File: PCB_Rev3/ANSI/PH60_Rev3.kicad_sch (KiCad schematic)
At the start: 28 parts, among them J1 USB_C_Receptacle_USB2.0_16P, J2 Conn_01x02, U1 XC6206PxxxMR, U2 W25Q16JVSS, U3 RP2040, Y1 Crystal_GND24

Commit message: Wires optimization.
More GND hole still needed...
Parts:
- J1: footprint Connector_USB:USB_C_Receptacle_HCTL_HC-TYPE-C-16P-01A -> PH60:USB-C_16P_HandSolder
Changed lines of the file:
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@@
 			)
 		)
-		(property "Footprint" "Connector_USB:USB_C_Receptacle_HCTL_HC-TYPE-C-16P-01A"
+		(property "Footprint" "PH60:USB-C_16P_HandSolder"
 			(at 52.07 220.98 0)
 			(effects

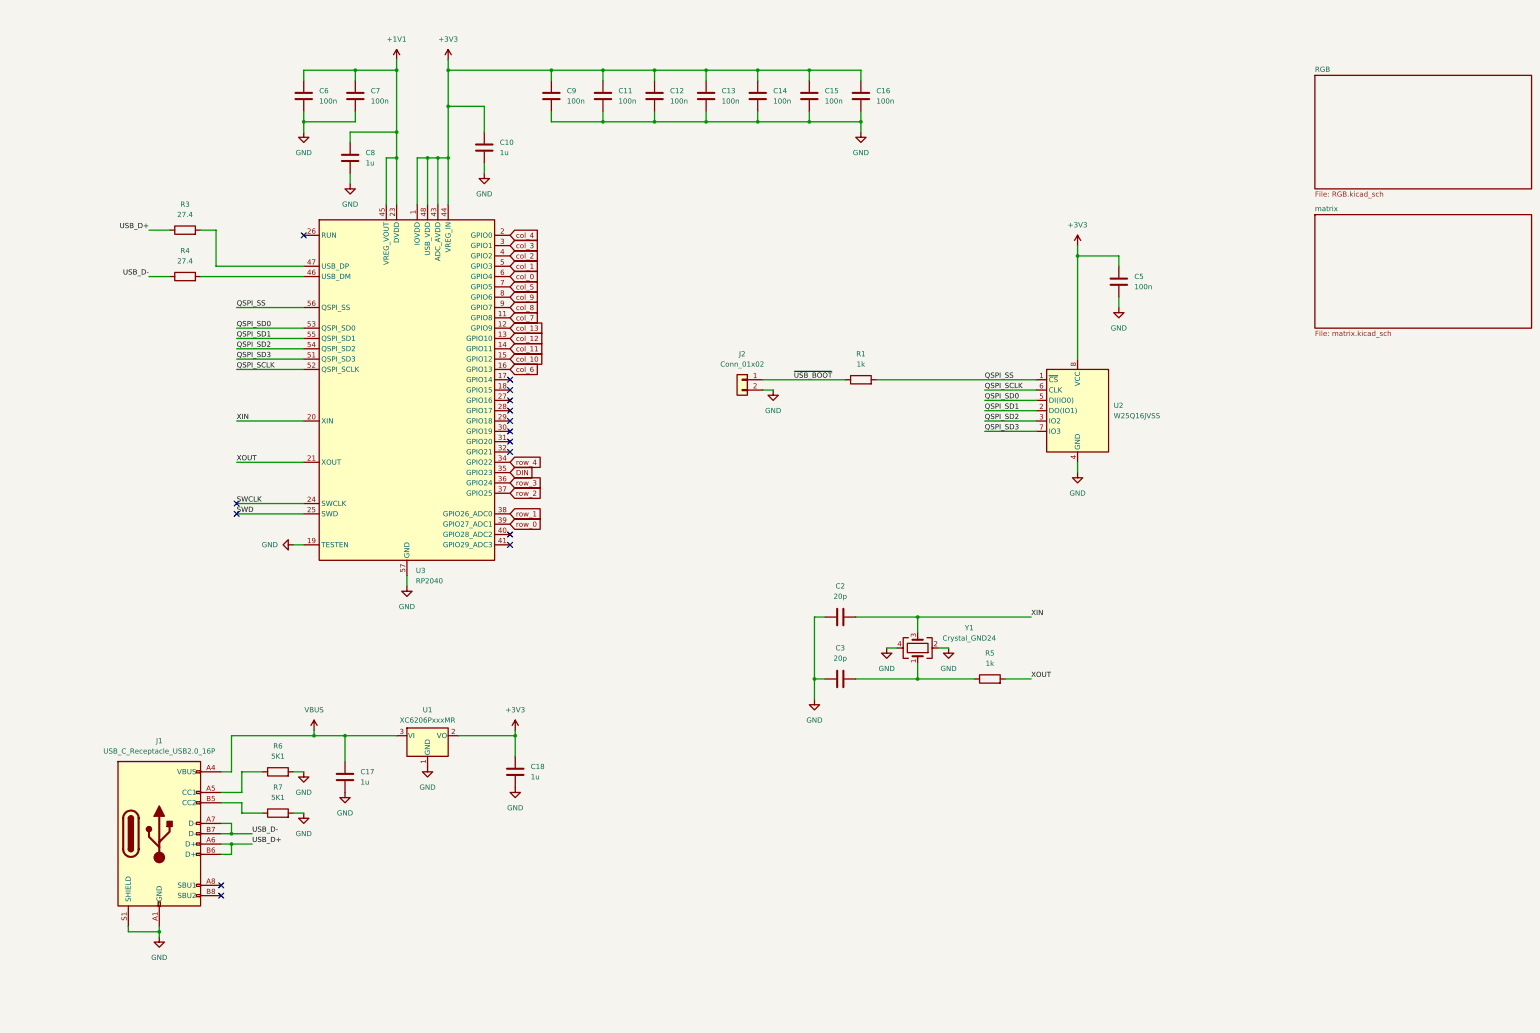
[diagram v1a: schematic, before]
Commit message: Add wireless part
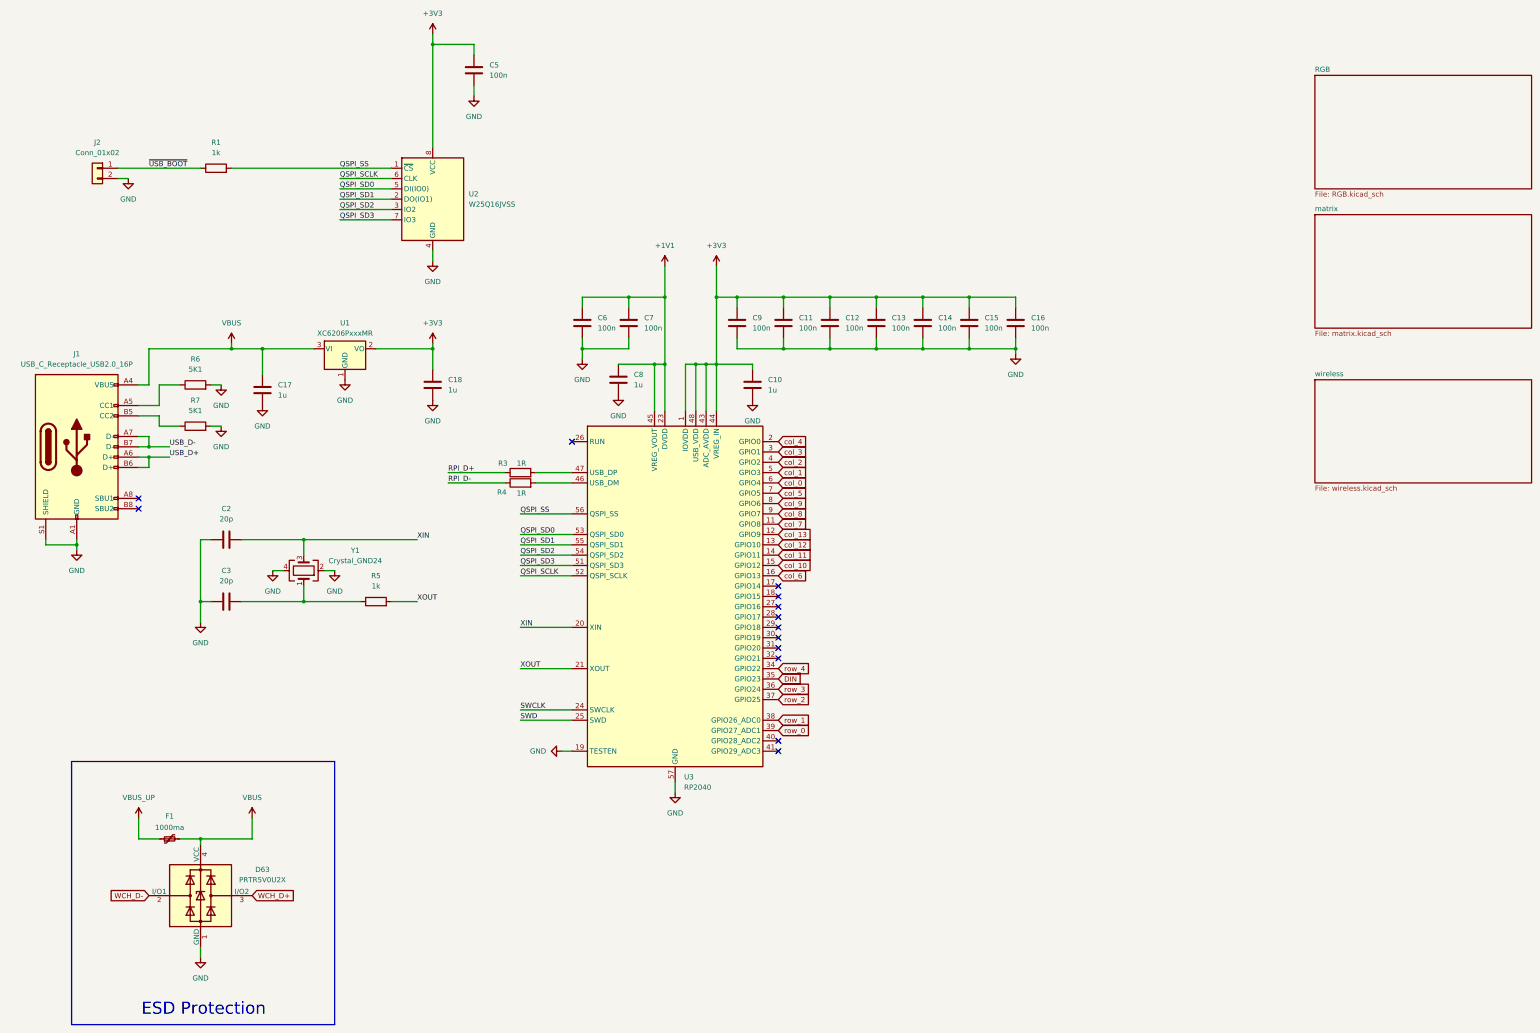
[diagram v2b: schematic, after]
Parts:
- added D63: PRTR5V0U2X, Package_TO_SOT_SMD:SOT-143, symbol Power_Protection:PRTR5V0U2X
- added F1: 1000ma, Fuse:Fuse_0805_2012Metric, symbol Device:Polyfuse_Small
- R3, R4: value 27.4 -> 1R
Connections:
- net GND: now also D63.1 (GND)
- net USB_D+: no longer R3.1
- net USB_D-: no longer R4.1
- net VBUS: now also D63.4 (VCC), F1.2
- new net RPI_D+: R3.1
- new net RPI_D-: R4.1
- new net VBUS_UP: F1.1
- new net WCH_D+: D63.3 (I/O2)
- new net WCH_D-: D63.2 (I/O1)
- no-connect marks 15 -> 13
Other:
- added sheet wireless (wireless.kicad_sch)
- note added: "ESD Protection"
- moved on the sheet: C10, C11, C12, C13, C14, C15, C16, C17, C18, C2, C3, C5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

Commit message: Finish board design
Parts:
- removed U1: XC6206PxxxMR, Package_TO_SOT_SMD:SOT-23-3, symbol Regulator_Linear:XC6206PxxxMR
- added BT1: Battery, Connector_Molex:Molex_PicoBlade_53261-0271_1x02-1MP_P1.25mm_Horizontal, symbol Device:Battery
- added C14: 4.7u, Capacitor_SMD:C_0402_1005Metric, symbol Device:C
- added C15: 10u, Capacitor_SMD:C_0402_1005Metric, symbol Device:C
- added J3: Conn_01x02_Pin, symbol Connector:Conn_01x02_Pin
- added J4: Conn_01x02_Pin, Connector_PinHeader_1.27mm:PinHeader_1x02_P1.27mm_Vertical, symbol Connector:Conn_01x02_Pin
- added L1, L2: 2.2uH, Inductor_SMD:L_Changjiang_FNR252012S, symbol Device:L
- added R10: 33k, PCM_Resistor_SMD_AKL:R_0402_1005Metric, symbol Device:R
- added R11: 10k, PCM_Resistor_SMD_AKL:R_0402_1005Metric, symbol Device:R
- added R12, R7: 100k, PCM_Resistor_SMD_AKL:R_0402_1005Metric, symbol Device:R
- added R6: 442k, PCM_Resistor_SMD_AKL:R_0402_1005Metric, symbol Device:R
- added R9: 1k, PCM_Resistor_SMD_AKL:R_0402_1005Metric, symbol Device:R
- added SW1: SW_SPDT_321, PCM_marbastlib-various:SW_MSK12C02-HB, symbol Switch:SW_SPDT_321
- added U1: TLV62569DBV, Package_TO_SOT_SMD:SOT-23-5, symbol Regulator_Switching:TLV62569DBV
- added U4: ETA6093, Package_TO_SOT_SMD:SOT-23-5, symbol ETA6093:ETA6093
- C17: value 1u -> 10u
- C18: value 1u -> 22u
- R1: renamed from R6; footprint Resistor_SMD:R_0402_1005Metric -> PCM_Resistor_SMD_AKL:R_0402_1005Metric
- R2: renamed from R7; footprint Resistor_SMD:R_0402_1005Metric -> PCM_Resistor_SMD_AKL:R_0402_1005Metric
- R3, R4, R5: footprint Resistor_SMD:R_0402_1005Metric -> PCM_Resistor_SMD_AKL:R_0402_1005Metric
- R8: renamed from R1; footprint Resistor_SMD:R_0402_1005Metric -> PCM_Resistor_SMD_AKL:R_0402_1005Metric
- renumbered C6 to C1, C8 to C10, C10 to C11, C2 to C12, C3 to C13, C5 to C16, C7 to C2, C9 to C3, C11 to C4, C12 to C5, C13 to C6, C14 to C7, C15 to C8, C16 to C9, D63 to D1, U3 to U2, U2 to U3
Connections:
- net WCH_D+ is gone; now on net USB_D-: D1.3 (I/O2)
- net WCH_D- is gone; now on net USB_D+: D1.2 (I/O1)
- net +3V3: now also C15.1, L1.2, R6.1; no longer C18.1
- net GND: now also BT1.2 (-), C14.2, C15.2, J4.2 (Pin_2), R12.2, R7.2, U1.2 (GND), U4.2 (GND)
- net SWCLK: now also J3.2 (Pin_2)
- net SWD: now also J3.1 (Pin_1)
- net VBUS: now also C18.1, C14.1, R11.2, U1.1 (EN), U1.4 (VIN), U4.1 (OUT); no longer C17.1, J1.A4 (VBUS), J1.A9 (VBUS), J1.B4 (VBUS), J1.B9 (VBUS)
- net VBUS_UP: now also J1.A4 (VBUS), J1.A9 (VBUS), J1.B4 (VBUS), J1.B9 (VBUS)
- net ~{USB_BOOT}: no longer names the net of J2.1 (Pin_1), R8.1
- new net: L1.1, U1.3 (SW)
- new net: R6.2, R7.1, U1.5 (FB)
- new net: C17.1, L2.1, SW1.3 (A), U4.4 (BAT)
- new net: R9.1, U4.3 (LED)
- new net: L2.2, U4.5 (SW)
- new net +BATT: BT1.1 (+), J4.1 (Pin_1), R10.2, SW1.2 (B)
- new net CHRG: R11.1, R9.2
- new net batt_level: R10.1, R12.1
- no-connect marks 13 -> 14
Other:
- note added: "Batt status"
- note added: "Charge & Boost"
- note added: "Crystal"
- note added: "Debug"
- note added: "Flash"
- note added: "RP2040"
- note added: "USB-C"
- note added: "power"
- moved on the sheet: C1, C10, C11, C12, C13, C16, C2, C3, C4, C5, C6, C7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

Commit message: Regroup
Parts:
- removed U3: W25Q16JVSS, Package_SON:Winbond_USON-8-1EP_3x2mm_P0.5mm_EP0.2x1.6mm, symbol Memory_Flash:W25Q16JVSS
- added U6: W25Q16JVSS, Package_SON:Winbond_USON-8-1EP_3x2mm_P0.5mm_EP0.2x1.6mm, symbol Memory_Flash:W25Q16JVSS
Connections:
- net QSPI_SS is gone; now on net RPI_BOOTSEL: R8.2, U2.56 (QSPI_SS)
- net +3V3: now also U6.8 (VCC)
- net GND: now also U6.4 (GND)
- net QSPI_SCLK: now also U6.6 (CLK)
- net QSPI_SD0: now also U6.5 (DI/IO_{0})
- net QSPI_SD1: now also U6.2 (DO/IO_{1})
- net QSPI_SD2: now also U6.3 (~{WP}/IO_{2})
- net QSPI_SD3: now also U6.7 (~{HOLD}/~{RESET}/IO_{3})
- net RPI_RUN: now reaches U2.26 (RUN)
- net RPI_BOOTSEL: now reaches J2.1 (Pin_1), R8.1
- net RPI_BOOTSEL: now also U6.1 (~{CS})
- no-connect marks 14 -> 13
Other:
- moved on the sheet: C14, C16, J2, R8

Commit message: Add files via upload
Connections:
- net +BATT: no longer SW1.2 (B)
- net GND: now also SW1.3 (A)
- net VBUS: now also SW1.1 (C); no longer U1.1 (EN)
- net at C17.1, L2.1, U4.4 (BAT): no longer SW1.3 (A)
- new net RGB: SW1.2 (B), U1.1 (EN)
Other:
- moved on the sheet: C14
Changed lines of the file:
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@@
 	)
 	(junction
-		(at 196.85 49.53)
+		(at 35.56 97.79)
 		(diameter 0)
 		(color 0 0 0 0)
 	)
 	(junction
-		(at 39.37 100.33)
+		(at 196.85 49.53)
 		(diameter 0)
 		(color 0 0 0 0)
@@
 	)
 	(junction
-		(at 80.01 38.1)
+		(at 45.72 102.87)
 		(diameter 0)
 		(color 0 0 0 0)
 	)
 	(junction
-		(at 146.05 53.34)
+		(at 80.01 38.1)
 		(diameter 0)
 		(color 0 0 0 0)
 	)
 	(junction
-		(at 53.34 154.94)
+		(at 146.05 53.34)
 		(diameter 0)
 		(color 0 0 0 0)
 	)
 	(junction
-		(at 39.37 97.79)
+		(at 53.34 154.94)
 		(diameter 0)
 		(color 0 0 0 0)
@@
 	)
 	(junction
+		(at 43.18 116.84)
+		(diameter 0)
+		(color 0 0 0 0)
+	)
+	(junction
 		(at 143.51 53.34)
 		(diameter 0)
@@
 	)
 	(junction
+		(at 33.02 97.79)
+		(diameter 0)
+		(color 0 0 0 0)
+	)
+	(junction
 		(at 226.06 152.4)
 		(diameter 0)
@@
 	(wire
 		(pts
-			(xy 39.37 97.79) (xy 45.72 97.79)
+			(xy 30.48 97.79) (xy 33.02 97.79)
 		)
 		(stroke
@@
 	(wire
 		(pts
-			(xy 39.37 100.33) (xy 39.37 97.79)
-		)
-		(stroke
-			(width 0)
-			(type default)
-		)
-	)
-	(wire
-		(pts
 			(xy 59.69 38.1) (xy 69.85 38.1)
 		)
@@
 	(wire
 		(pts
+			(xy 33.02 97.79) (xy 35.56 97.79)
+		)
+		(stroke
+			(width 0)
+			(type default)
+		)
+	)
+	(wire
+		(pts
 			(xy 80.01 35.56) (xy 80.01 38.1)
 		)
@@
 	(wire
 		(pts
-			(xy 39.37 102.87) (xy 39.37 100.33)
+			(xy 33.02 97.79) (xy 33.02 102.87)
 		)
 		(stroke
@@
 	(wire
 		(pts
+			(xy 35.56 97.79) (xy 35.56 113.03)
+		)
+		(stroke
+			(width 0)
+			(type default)
+		)
+	)
+	(wire
+		(pts
 			(xy 53.34 223.52) (xy 53.34 227.33)
 		)
@@
 	(wire
 		(pts
-			(xy 39.37 116.84) (xy 53.34 116.84)
+			(xy 33.02 116.84) (xy 43.18 116.84)
 		)
 		(stroke
@@
 	(wire
 		(pts
+			(xy 40.64 102.87) (xy 45.72 102.87)
+		)
+		(stroke
+			(width 0)
+			(type default)
+		)
+	)
+	(wire
+		(pts
 			(xy 73.66 237.49) (xy 73.66 234.95)
 		)
@@
 	(wire
 		(pts
+			(xy 43.18 116.84) (xy 53.34 116.84)
+		)
+		(stroke
+			(width 0)
+			(type default)
+		)
+	)
+	(wire
+		(pts
 			(xy 162.56 36.83) (xy 162.56 39.37)
 		)
@@
 	(wire
 		(pts
-			(xy 39.37 100.33) (xy 45.72 100.33)
-		)
-		(stroke
-			(width 0)
-			(type default)
-		)
-	)
-	(wire
-		(pts
 			(xy 63.5 107.95) (xy 71.12 107.95)
 		)
@@
 	(wire
 		(pts
-			(xy 30.48 97.79) (xy 39.37 97.79)
-		)
-		(stroke
-			(width 0)
-			(type default)
-		)
-	)
-	(wire
-		(pts
 			(xy 146.05 36.83) (xy 151.13 36.83)
 		)
@@
 	(wire
 		(pts
-			(xy 39.37 116.84) (xy 39.37 110.49)
+			(xy 33.02 116.84) (xy 33.02 110.49)
 		)
 		(stroke
@@
 	(wire
 		(pts
+			(xy 43.18 113.03) (xy 43.18 116.84)
+		)
+		(stroke
+			(width 0)
+			(type default)
+		)
+	)
+	(wire
+		(pts
+			(xy 45.72 102.87) (xy 45.72 100.33)
+		)
+		(stroke
+			(width 0)
+			(type default)
+		)
+	)
+	(wire
+		(pts
 			(xy 36.83 68.58) (xy 36.83 69.85)
 		)
@@
 	(wire
 		(pts
+			(xy 45.72 107.95) (xy 45.72 102.87)
+		)
+		(stroke
+			(width 0)
+			(type default)
+		)
+	)
+	(wire
+		(pts
 			(xy 226.06 152.4) (xy 226.06 153.67)
 		)
@@
 	(wire
 		(pts
+			(xy 35.56 97.79) (xy 45.72 97.79)
+		)
+		(stroke
+			(width 0)
+			(type default)
+		)
+	)
+	(wire
+		(pts
 			(xy 30.48 226.06) (xy 40.64 226.06)
 		)
@@
 	(wire
 		(pts
+			(xy 38.1 113.03) (xy 35.56 113.03)
+		)
+		(stroke
+			(width 0)
+			(type default)
+		)
+	)
+	(wire
+		(pts
 			(xy 121.92 53.34) (xy 130.81 53.34)
 		)
@@
 	(symbol
 		(lib_id "Device:C")
-		(at 39.37 106.68 0)
+		(at 33.02 106.68 0)
 		(unit 1)
 		(exclude_from_sim no)
@@
 		(fields_autoplaced yes)
 		(property "Reference" "C14"
-			(at 43.18 105.4099 0)
+			(at 36.83 105.4099 0)
 			(effects
 				(font
@@
 		)
 		(property "Value" "4.7u"
-			(at 43.18 107.9499 0)
+			(at 36.83 107.9499 0)
 			(effects
 				(font
@@
 		)
 		(property "Footprint" "Capacitor_SMD:C_0402_1005Metric"
-			(at 40.3352 110.49 0)
+			(at 33.9852 110.49 0)
 			(effects
 				(font
@@
 		)
 		(property "Datasheet" "~"
-			(at 39.37 106.68 0)
+			(at 33.02 106.68 0)
 			(effects
 				(font
@@
 		)
 		(property "Description" "Unpolarized capacitor"
-			(at 39.37 106.68 0)
+			(at 33.02 106.68 0)
 			(effects
 				(font
@@
 	(symbol
 		(lib_id "Switch:SW_SPDT_321")
-		(at 48.26 226.06 0)
+		(at 40.64 107.95 270)
 		(unit 1)
 		(exclude_from_sim no)
@@
 		(on_board yes)
 		(dnp no)
-		(fields_autoplaced yes)
 		(property "Reference" "SW1"
-			(at 48.26 217.17 0)
+			(at 37.592 98.552 90)
 			(effects
 				(font
 					(size 1.27 1.27)
 				)
+				(justify left)
+				(hide yes)
 			)
 		)
 		(property "Value" "SW_SPDT_321"
-			(at 48.26 219.71 0)
+			(at 17.78 101.854 90)
 			(effects
 				(font
 					(size 1.27 1.27)
 				)
+				(justify left)
+				(hide yes)
 			)
 		)
 		(property "Footprint" "PCM_marbastlib-various:SW_MSK12C02-HB"
-			(at 48.26 236.22 0)
+			(at 30.48 107.95 0)
 			(effects
 				(font
@@
 		)
 		(property "Datasheet" "~"
-			(at 48.26 233.68 0)
+			(at 33.02 107.95 0)
 			(effects
 				(font
@@
 		)
 		(property "Description" "Switch, single pole double throw"
-			(at 48.26 226.06 0)
+			(at 40.64 107.95 0)
 			(effects
 				(font
@@
 					(unit 1)
 				)
+			)
+		)
+	)
+	(symbol
+		(lib_id "power:VBUS")
+		(at 45.72 107.95 180)
+		(unit 1)
+		(exclude_from_sim no)
+		(in_bom yes)
+		(on_board yes)
+		(dnp no)
+		(property "Reference" "#PWR037"
+			(at 45.72 104.14 0)
+			(effects
+				(font
+					(size 1.27 1.27)
+				)
+				(hide yes)
+			)
+		)
+		(property "Value" "RGB"
+			(at 48.006 109.22 0)
+			(effects
+				(font
+					(size 1.27 1.27)
+				)
+				(justify right)
+			)
+		)
+		(property "Footprint" ""
+			(at 45.72 107.95 0)
+			(effects
+				(font
+					(size 1.27 1.27)
+				)
+				(hide yes)
+			)
+		)
+		(property "Datasheet" ""
+			(at 45.72 107.95 0)
+			(effects
+				(font
+					(size 1.27 1.27)
+				)
+				(hide yes)
+			)
+		)
+		(property "Description" "Power symbol creates a global label with name \"VBUS\""
+			(at 45.72 107.95 0)
+			(effects
+				(font
+					(size 1.27 1.27)
+				)
+				(hide yes)
+			)
+		)
+		(pin "1"
+		)
+		(instances
+			(project "PH60_Rev3"
+				(path "/dca0f898-8fdb-4522-a51d-f4f4238906e7"
+					(reference "#PWR037")
+					(unit 1)
+				)

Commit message: Add files via upload
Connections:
- net RPI_BOOTSEL: no longer R8.2, U2.56 (QSPI_SS), U6.1 (~{CS})
- new net QSPI_SS: R8.2, U2.56 (QSPI_SS), U6.1 (~{CS})
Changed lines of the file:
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@@
-	)
-	(junction
-		(at 201.93 132.08)
-		(diameter 0)
-		(color 0 0 0 0)
 	)
 	(junction
@@
 	(junction
 		(at 99.06 219.71)
-		(diameter 0)
-		(color 0 0 0 0)
-	)
-	(junction
-		(at 194.31 132.08)
 		(diameter 0)
 		(color 0 0 0 0)
@@
 	(wire
 		(pts
-			(xy 201.93 132.08) (xy 194.31 132.08)
-		)
-		(stroke
-			(width 0)
-			(type default)
-		)
-	)
-	(wire
-		(pts
 			(xy 95.25 219.71) (xy 99.06 219.71)
 		)
@@
 	(wire
 		(pts
+			(xy 194.31 132.08) (xy 194.31 152.4)
+		)
+		(stroke
+			(width 0)
+			(type default)
+		)
+	)
+	(wire
+		(pts
 			(xy 30.48 237.49) (xy 40.64 237.49)
 		)
@@
 		)
 		(stroke
-			(width 0)
-			(type default)
-		)
-	)
-	(wire
-		(pts
-			(xy 194.31 152.4) (xy 194.31 132.08)
-		)
-		(stroke

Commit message: Finish board design
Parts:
- U2: footprint Package_DFN_QFN:QFN-56-1EP_7x7mm_P0.4mm_EP3.2x3.2mm_ThermalVias -> Package_DFN_QFN:QFN-56-1EP_7x7mm_P0.4mm_EP3.2x3.2mm
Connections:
- net +BATT: now also C17.1, L2.1, U4.4 (BAT)
- net VBUS: no longer U1.4 (VIN)
- net RGB renamed VBUS_SW
- net VBUS_SW: now also U1.4 (VIN)
- no-connect marks 13 -> 12
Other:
- moved on the sheet: C14
